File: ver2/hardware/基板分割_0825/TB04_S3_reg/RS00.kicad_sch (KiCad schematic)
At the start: 20 parts, among them IC201 74HC161N, IC202 74HC161N, IC203 74HC161N, IC204 74HC161N, J201 Conn_02x05_Odd_Even, J202 Conn_02x05_Odd_Even, J203 Conn_02x05_Odd_Even, J204 Conn_02x05_Odd_Even, U201 74LS253, U202 74LS253, U203 74LS253, U204 74LS253

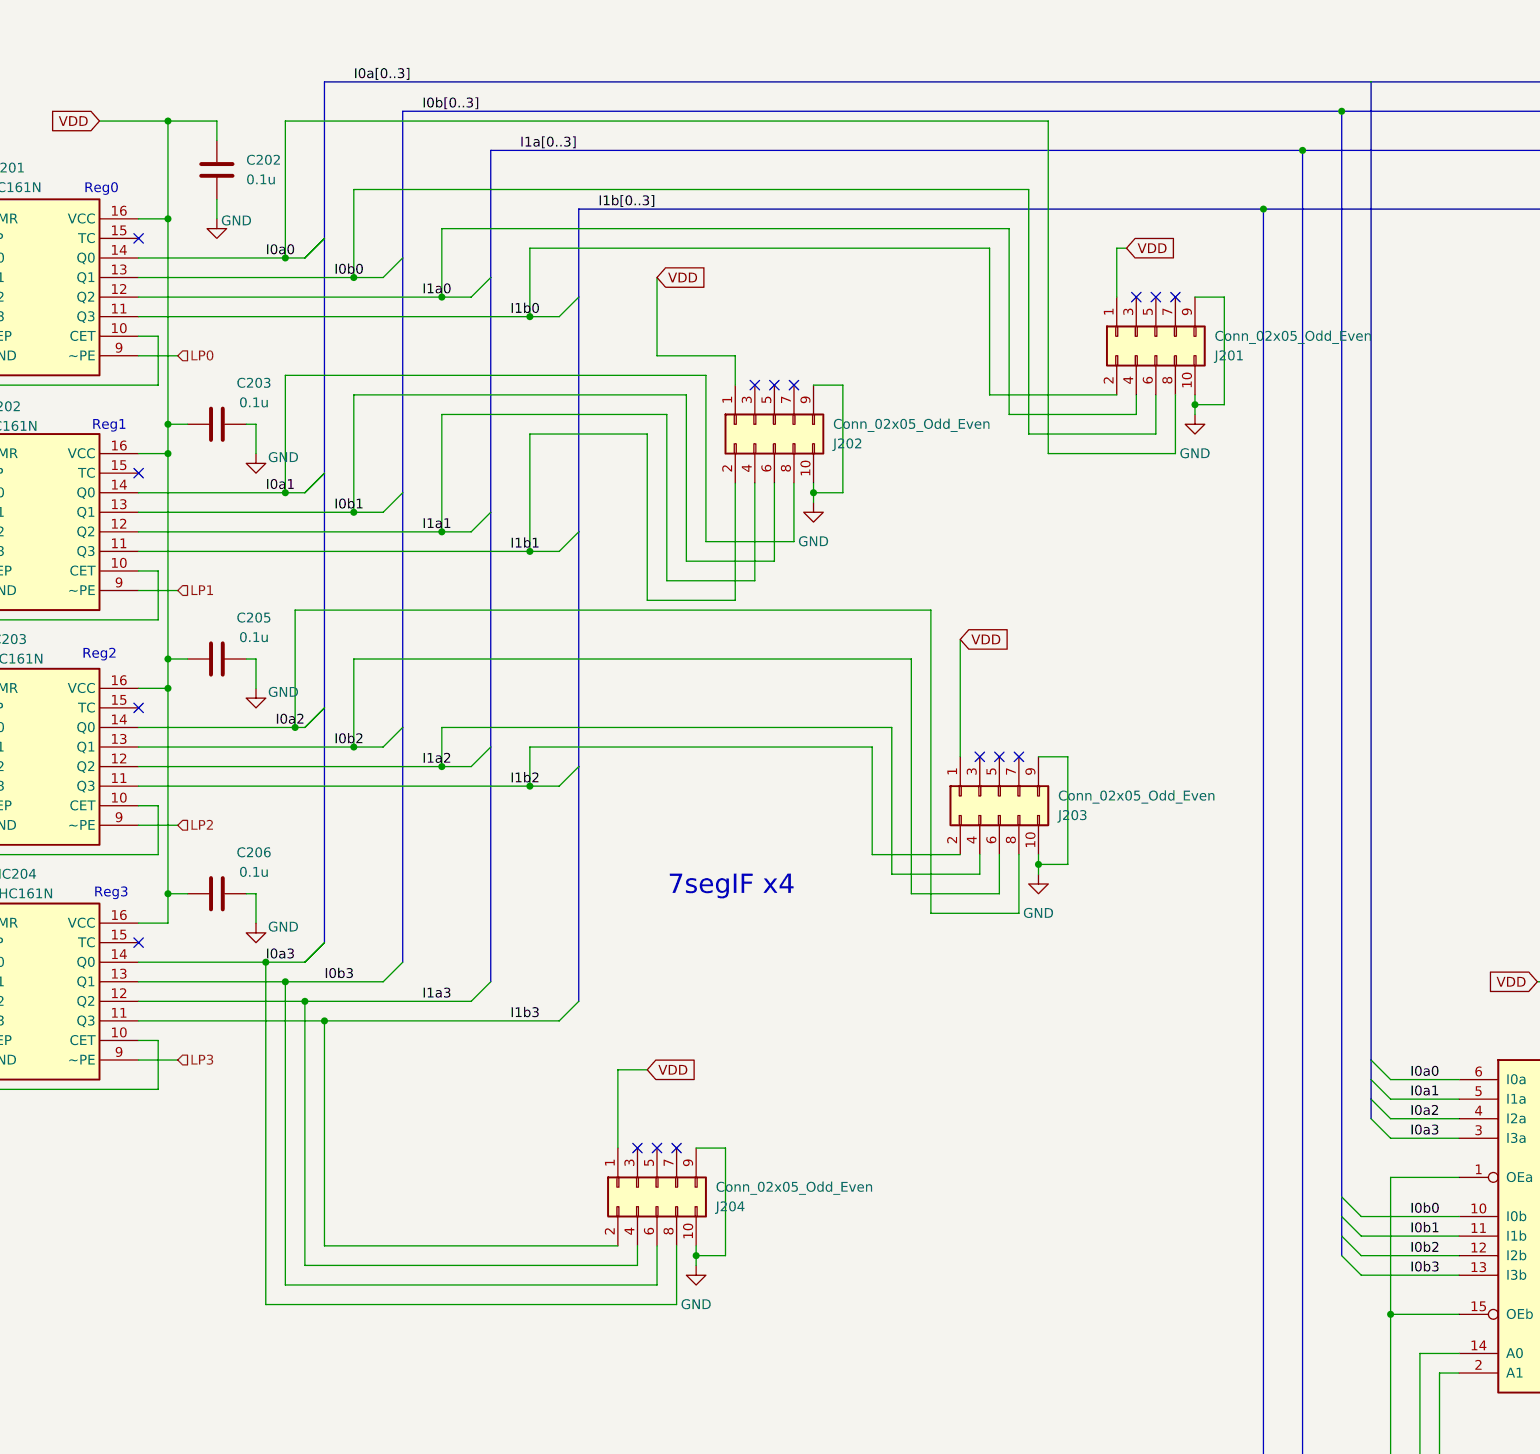
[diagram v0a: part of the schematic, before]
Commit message: ver2: S1-S4にバスヘッダ3本を実装(120ピン全数一致)／S4にIF向け20ピン3個
J101-103は4枚とも確定表と全120ピン一致。J104(IF入力)/J105(IF表示)/
J106(キャリアB)も20ピン全一致。コネクタ以外の署名はマスターと相違0で、
コネクタ追加時のワイヤ吸着なし。PC_Qはバスに載せずJ106のみ。

Co-Authored-By: Claude Opus 5 <noreply@anthropic.com>
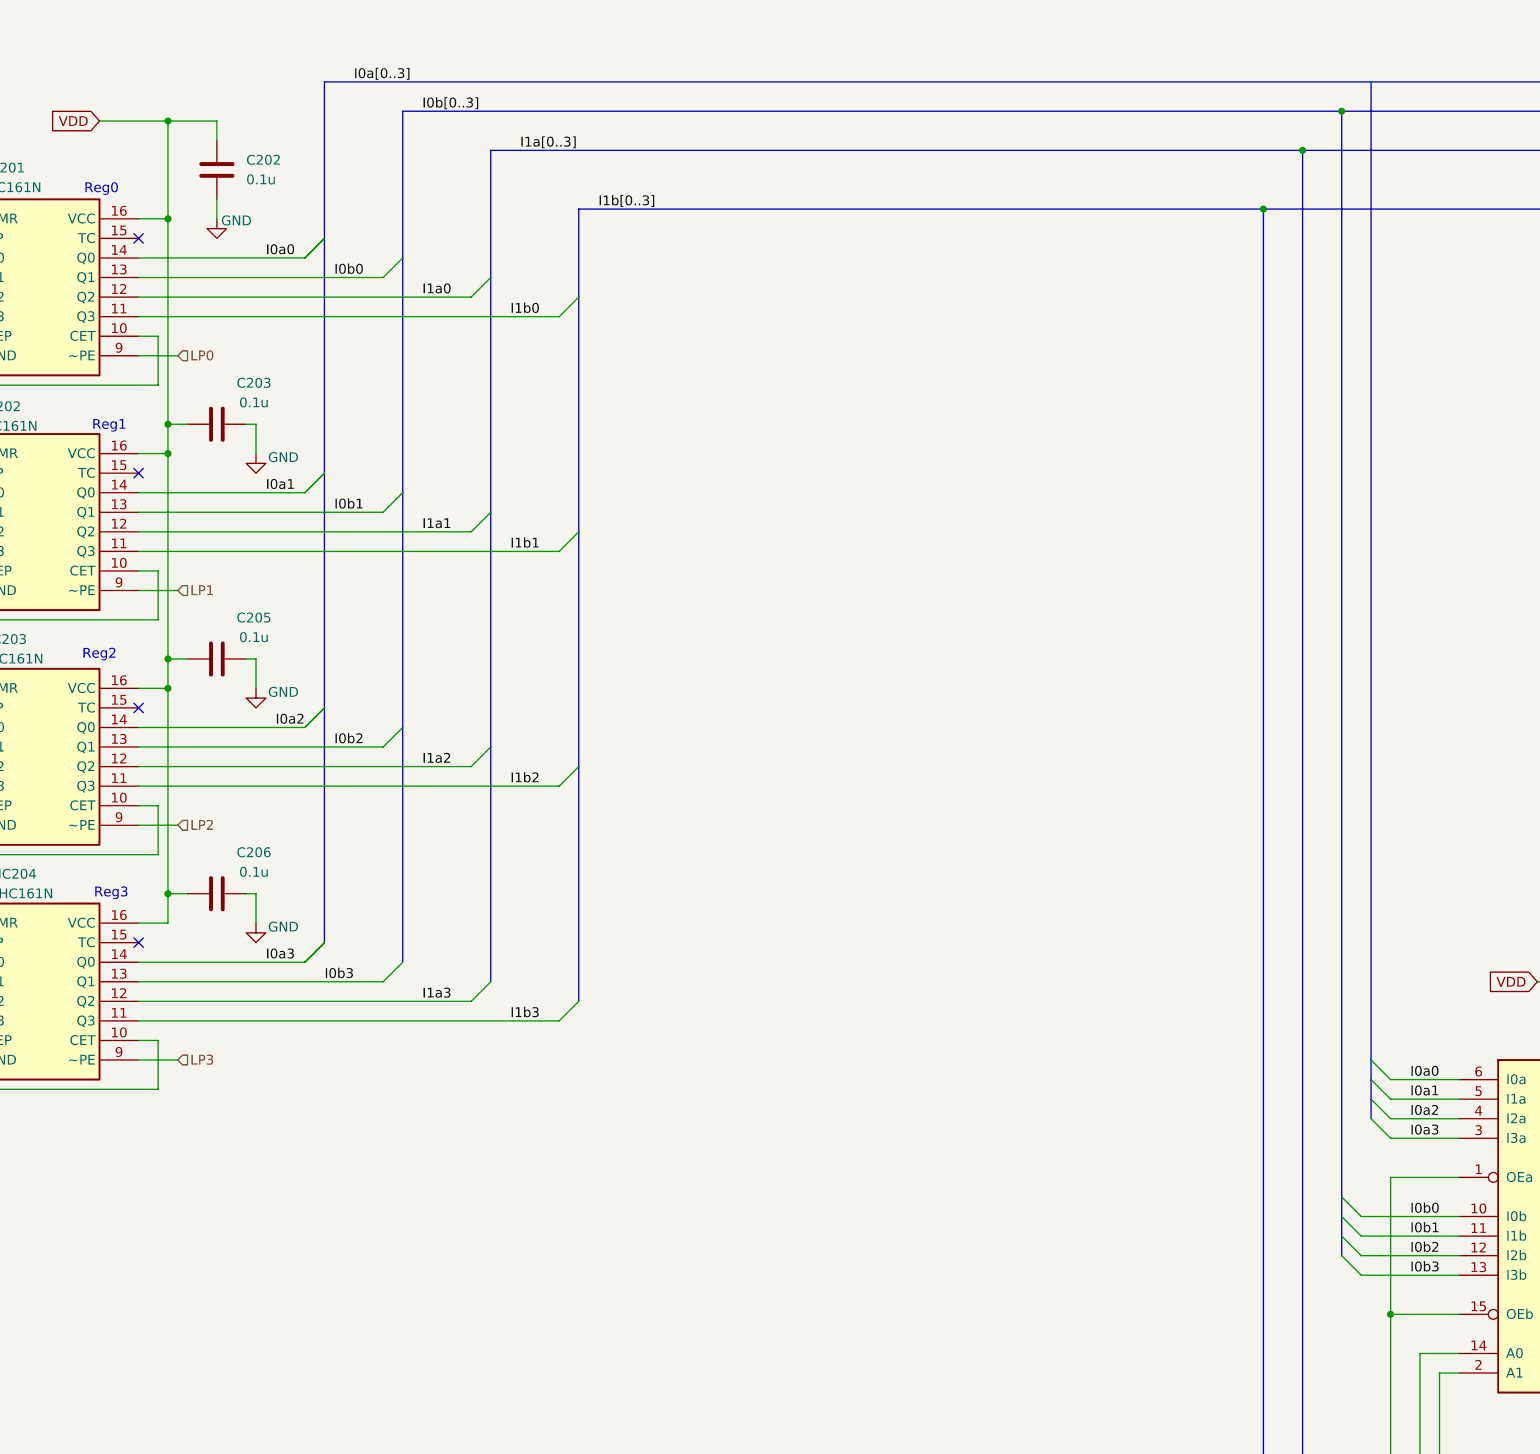
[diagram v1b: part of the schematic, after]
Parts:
- removed J201, J202, J203, J204: Conn_02x05_Odd_Even, symbol Connector_Generic:Conn_02x05_Odd_Even
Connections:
- no-connect marks 16 -> 4
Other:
- note removed: "7segIF x4"
